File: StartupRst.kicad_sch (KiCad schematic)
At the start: 6 parts, among them Q4 DMN10H220L, Q5 DMN10H220L

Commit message: minor changes
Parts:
- added R52: 10k, Resistor_SMD:R_0805_2012Metric, symbol Device:R
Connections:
- net RST_: now also R52.1
- new net +3V3: R52.2
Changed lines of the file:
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@@
+	)
+	(junction
+		(at 154.94 48.26)
+		(diameter 0)
+		(color 0 0 0 0)
 	)
 	(junction
@@
 	(wire
 		(pts
+			(xy 154.94 48.26) (xy 182.88 48.26)
+		)
+		(stroke
+			(width 0)
+			(type default)
+		)
+	)
+	(wire
+		(pts
 			(xy 206.375 40.005) (xy 206.375 45.085)
 		)
@@
 	(wire
 		(pts
+			(xy 154.94 27.94) (xy 154.94 30.48)
+		)
+		(stroke
+			(width 0)
+			(type default)
+		)
+	)
+	(wire
+		(pts
 			(xy 59.055 66.04) (xy 59.055 76.2)
 		)
@@
 	(wire
 		(pts
+			(xy 154.94 38.1) (xy 154.94 48.26)
+		)
+		(stroke
+			(width 0)
+			(type default)
+		)
+	)
+	(wire
+		(pts
 			(xy 74.295 81.915) (xy 74.295 89.535)
 		)
@@
 	(wire
 		(pts
-			(xy 106.68 48.26) (xy 182.88 48.26)
+			(xy 106.68 48.26) (xy 154.94 48.26)
 		)
 		(stroke
@@
 	)
 	(symbol
+		(lib_id "Device:R")
+		(at 154.94 34.29 180)
+		(unit 1)
+		(exclude_from_sim no)
+		(in_bom yes)
+		(on_board yes)
+		(dnp no)
+		(property "Reference" "R52"
+			(at 152.4 38.1 90)
+			(effects
+				(font
+					(size 1.27 1.27)
+				)
+			)
+		)
+		(property "Value" "10k"
+			(at 152.7326 34.29 90)
+			(effects
+				(font
+					(size 1.27 1.27)
+				)
+			)
+		)
+		(property "Footprint" "Resistor_SMD:R_0805_2012Metric"
+			(at 156.718 34.29 90)
+			(effects
+				(font
+					(size 1.27 1.27)
+				)
+				(hide yes)
+			)
+		)
+		(property "Datasheet" "~"
+			(at 154.94 34.29 0)
+			(effects
+				(font
+					(size 1.27 1.27)
+				)
+				(hide yes)
+			)
+		)
+		(property "Description" ""
+			(at 154.94 34.29 0)
+			(effects
+				(font
+					(size 1.27 1.27)
+				)
+				(hide yes)
+			)
+		)
+		(pin "1"
+		)
+		(pin "2"
+		)
+		(instances
+			(project "TPA3255PBTL"
+				(path "/ffe003c3-62df-4c03-9b6a-8506f1ae9e28/d2d9f304-0e95-4703-8f1b-74aeca3b53bb"
+					(reference "R52")
+					(unit 1)
+				)
+			)
+		)
+	)
+	(symbol
 		(lib_id "power:GND")
 		(at 206.375 48.26 0)
@@
 					(unit 1)
 				)
+			)
+		)
+	)
+	(symbol
+		(lib_id "power:+3.3V")
+		(at 154.94 27.94 0)
+		(unit 1)
+		(exclude_from_sim no)
+		(in_bom yes)
+		(on_board yes)
+		(dnp no)
+		(fields_autoplaced yes)
+		(property "Reference" "#PWR05"
+			(at 154.94 31.75 0)
+			(effects
+				(font
+					(size 1.27 1.27)
+				)
+				(hide yes)
+			)
+		)
+		(property "Value" "+3V3"
+			(at 154.94 24.3355 0)
+			(effects
+				(font
+					(size 1.27 1.27)
+				)
+			)
+		)
+		(property "Footprint" ""
+			(at 154.94 27.94 0)
+			(effects
+				(font
+					(size 1.27 1.27)
+				)
+				(hide yes)
+			)
+		)
+		(property "Datasheet" ""
+			(at 154.94 27.94 0)
+			(effects
+				(font
+					(size 1.27 1.27)
+				)
+				(hide yes)
+			)
+		)
+		(property "Description" ""
+			(at 154.94 27.94 0)
+			(effects
+				(font
+					(size 1.27 1.27)
+				)
+				(hide yes)
+			)
+		)
+		(pin "1"
+		)
+		(instances
+			(project "TPA3255PBTL"
+				(path "/ffe003c3-62df-4c03-9b6a-8506f1ae9e28/d2d9f304-0e95-4703-8f1b-74aeca3b53bb"
+					(reference "#PWR05")
+					(unit 1)
+				)

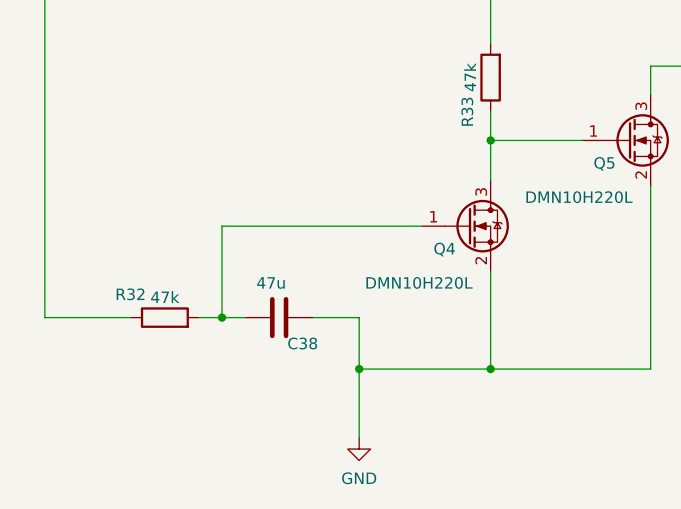
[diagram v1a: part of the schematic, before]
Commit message: Add testing/ update README/ Current control
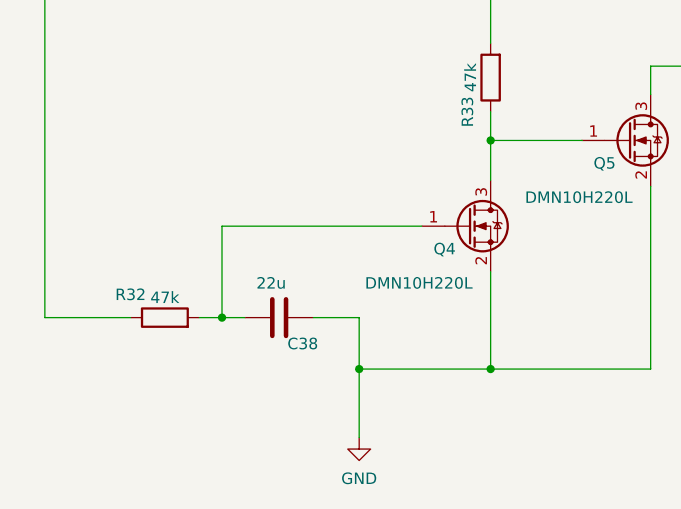
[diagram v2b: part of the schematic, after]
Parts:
- C38: value 47u -> 22u
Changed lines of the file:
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@@
 			)
 		)
-		(property "Value" "47u"
+		(property "Value" "22u"
 			(at 62.865 72.39 90)
 			(effects
